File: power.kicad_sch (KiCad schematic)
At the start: 58 parts, among them U3 AP2112K-3.3, U4 LM317_TO-252, U5 LMR36520FADDA, U6 CJ431, U8 CJ431, U9 LMR36520FADDA

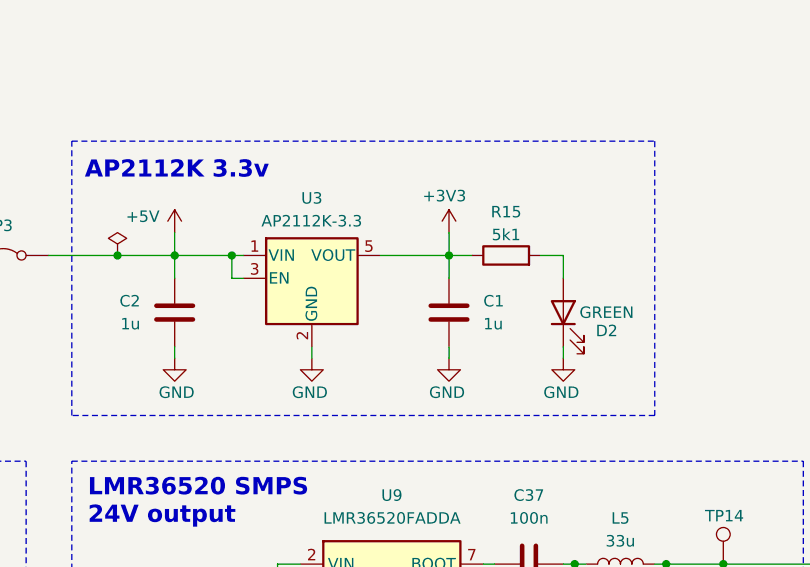
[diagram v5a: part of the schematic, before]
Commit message: schem: add +3V3 test point
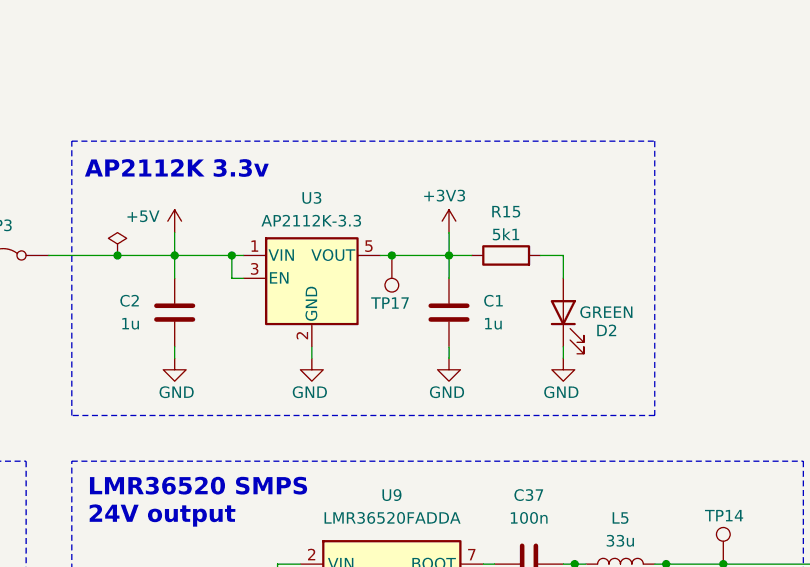
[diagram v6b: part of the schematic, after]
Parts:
- added TP17: TestPoint, symbol Connector:TestPoint
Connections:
- net +3V3: now also TP17.1
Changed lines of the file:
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@@
 	)
 	(junction
+		(at 213.36 91.44)
+		(diameter 0)
+		(color 0 0 0 0)
+	)
+	(junction
 		(at 100.33 128.27)
 		(diameter 0)
@@
 	(wire
 		(pts
+			(xy 213.36 91.44) (xy 219.71 91.44)
+		)
+		(stroke
+			(width 0)
+			(type default)
+		)
+	)
+	(wire
+		(pts
 			(xy 109.22 49.53) (xy 109.22 57.15)
 		)
@@
 	(wire
 		(pts
-			(xy 212.09 91.44) (xy 219.71 91.44)
+			(xy 212.09 91.44) (xy 213.36 91.44)
 		)
 		(stroke
@@
 					(unit 1)
 				)
+			)
+		)
+	)
+	(symbol
+		(lib_id "Connector:TestPoint")
+		(at 213.36 91.44 180)
+		(unit 1)
+		(exclude_from_sim no)
+		(in_bom yes)
+		(on_board yes)
+		(dnp no)
+		(property "Reference" "TP17"
+			(at 215.392 96.774 0)
+			(effects
+				(font
+					(size 1.27 1.27)
+				)
+				(justify left)
+			)
+		)
+		(property "Value" "TestPoint"
+			(at 210.82 93.4721 0)
+			(effects
+				(font
+					(size 1.27 1.27)
+				)
+				(justify left)
+				(hide yes)
+			)
+		)
+		(property "Footprint" ""
+			(at 208.28 91.44 0)
+			(effects
+				(font
+					(size 1.27 1.27)
+				)
+				(hide yes)
+			)
+		)
+		(property "Datasheet" "~"
+			(at 208.28 91.44 0)
+			(effects
+				(font
+					(size 1.27 1.27)
+				)
+				(hide yes)
+			)
+		)
+		(property "Description" "test point"
+			(at 213.36 91.44 0)
+			(effects
+				(font
+					(size 1.27 1.27)
+				)
+				(hide yes)
+			)
+		)
+		(pin "1"
+		)
+		(instances
+			(project "esp32c6-sensor-devboard"
+				(path "/f6edeef8-7fa0-4f55-9ad8-145372f41e3e/4befa429-10a8-402a-b91d-1560a39651d5"
+					(reference "TP17")
+					(unit 1)
+				)

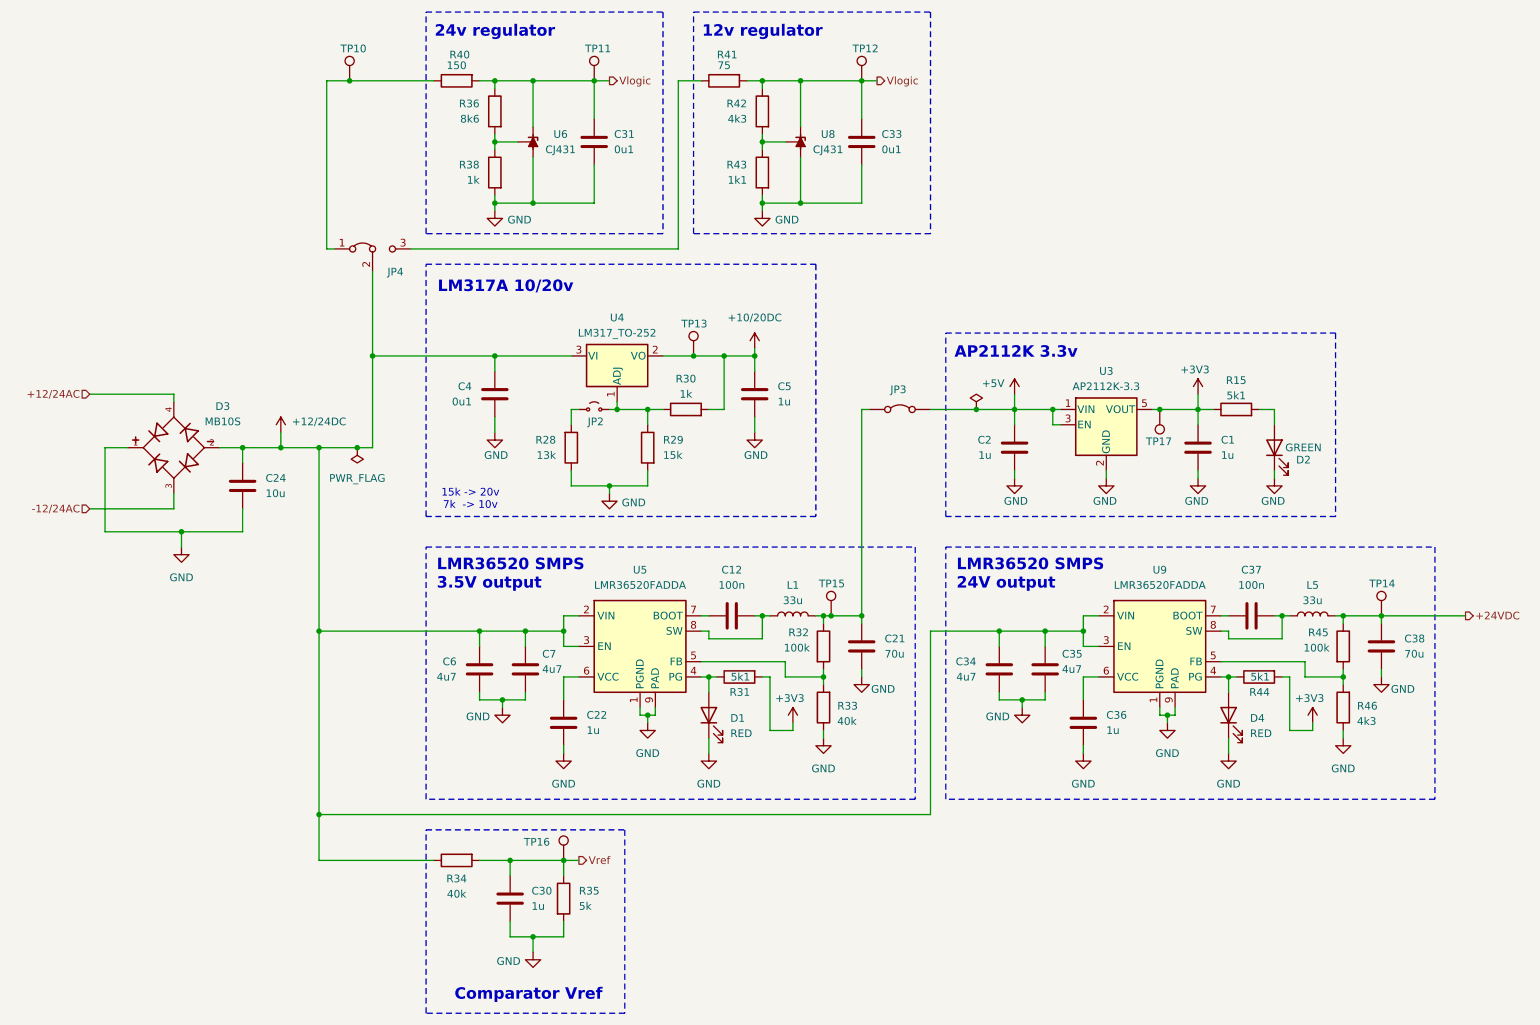
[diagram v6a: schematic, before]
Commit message: schem: assign footprints
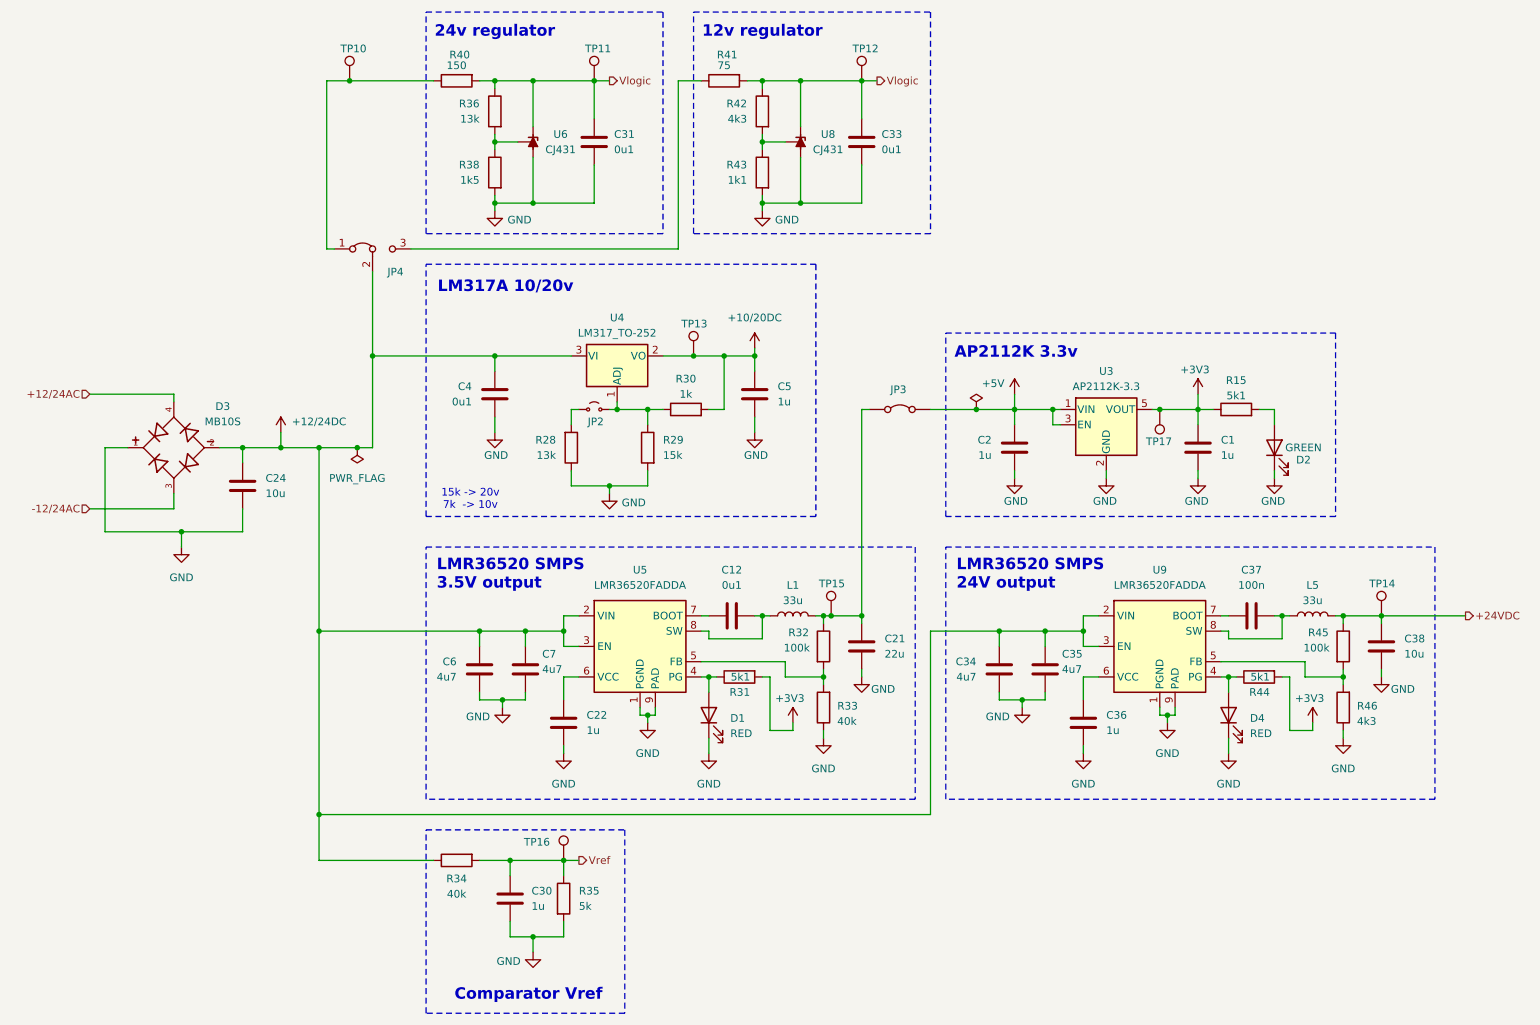
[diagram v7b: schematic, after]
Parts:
- C1, C2, C24, C4, C5: footprint (none) -> Capacitor_SMD:C_0603_1608Metric
- C12: value 100n -> 0u1; footprint (none) -> Capacitor_SMD:C_0402_1005Metric
- C21: value 70u -> 22u; footprint (none) -> Capacitor_SMD:C_0603_1608Metric
- C22, C30, C31, C33, C36, C37: footprint (none) -> Capacitor_SMD:C_0402_1005Metric
- C34, C35, C6, C7: footprint (none) -> Capacitor_SMD:C_1206_3216Metric
- C38: value 70u -> 10u; footprint (none) -> Capacitor_SMD:C_0603_1608Metric
- D1, D4: footprint (none) -> LED_SMD:LED_0603_1608Metric
- JP2, JP3: footprint (none) -> Connector_PinHeader_2.54mm:PinHeader_1x02_P2.54mm_Vertical
- JP4: footprint (none) -> Connector_PinHeader_2.54mm:PinHeader_1x03_P2.54mm_Vertical
- L1, L5: footprint (none) -> Inductor_SMD:L_Chilisin_BMRx00060630
- R15, R28, R29, R30, R31, R32, R33, R34, R35, R42, R43, R44, R45, R46: footprint (none) -> Resistor_SMD:R_0603_1608Metric
- R36: value 8k6 -> 13k; footprint (none) -> Resistor_SMD:R_0603_1608Metric
- R38: value 1k -> 1k5; footprint (none) -> Resistor_SMD:R_0603_1608Metric
- R40, R41: footprint (none) -> Resistor_SMD:R_0805_2012Metric
- TP10, TP11, TP12, TP13, TP14, TP15, TP16, TP17: footprint (none) -> TestPoint:TestPoint_Pad_D2.0mm
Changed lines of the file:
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@@
 			)
 		)
-		(property "Footprint" ""
+		(property "Footprint" "TestPoint:TestPoint_Pad_D2.0mm"
 			(at 255.27 125.73 0)
 			(effects
@@
 			)
 		)
-		(property "Footprint" ""
+		(property "Footprint" "Resistor_SMD:R_0805_2012Metric"
 			(at 140.97 35.052 90)
 			(effects
@@
 			)
 		)
-		(property "Footprint" ""
+		(property "Footprint" "Resistor_SMD:R_0603_1608Metric"
 			(at 113.792 97.79 90)
 			(effects
@@
 			)
 		)
-		(property "Footprint" ""
+		(property "Footprint" "Connector_PinHeader_2.54mm:PinHeader_1x02_P2.54mm_Vertical"
 			(at 119.38 91.44 0)
 			(effects
@@
 			)
 		)
-		(property "Value" "8k6"
+		(property "Value" "13k"
 			(at 100.33 43.1799 0)
 			(effects
@@
 			)
 		)
-		(property "Footprint" ""
+		(property "Footprint" "Resistor_SMD:R_0603_1608Metric"
 			(at 104.648 41.91 90)
 			(effects
@@
 			)
 		)
-		(property "Footprint" ""
+		(property "Footprint" "Resistor_SMD:R_0603_1608Metric"
 			(at 96.52 164.592 90)
 			(effects
@@
 			)
 		)
-		(property "Footprint" ""
+		(property "Footprint" "TestPoint:TestPoint_Pad_D2.0mm"
 			(at 140.97 82.55 0)
 			(effects
@@
 			)
 		)
-		(property "Footprint" ""
+		(property "Footprint" "Capacitor_SMD:C_0402_1005Metric"
 			(at 106.3752 176.53 0)
 			(effects
@@
 			)
 		)
-		(property "Footprint" ""
+		(property "Footprint" "Capacitor_SMD:C_1206_3216Metric"
 			(at 108.9152 138.43 0)
 			(effects
@@
 			)
 		)
-		(property "Footprint" ""
+		(property "Footprint" "Resistor_SMD:R_0603_1608Metric"
 			(at 226.06 93.218 90)
 			(effects
@@
 			)
 		)
-		(property "Footprint" ""
+		(property "Footprint" "Capacitor_SMD:C_0603_1608Metric"
 			(at 220.6752 101.6 0)
 			(effects
@@
 			)
 		)
-		(property "Footprint" ""
+		(property "Footprint" "Resistor_SMD:R_0603_1608Metric"
 			(at 245.618 140.97 90)
 			(effects
@@
 			)
 		)
-		(property "Footprint" ""
+		(property "Footprint" "TestPoint:TestPoint_Pad_D2.0mm"
 			(at 119.38 166.37 0)
 			(effects
@@
 			)
 		)
-		(property "Footprint" ""
+		(property "Footprint" "LED_SMD:LED_0603_1608Metric"
 			(at 224.79 142.24 0)
 			(effects
@@
 			)
 		)
-		(property "Footprint" ""
+		(property "Footprint" "TestPoint:TestPoint_Pad_D2.0mm"
 			(at 163.83 125.73 0)
 			(effects
@@
 			)
 		)
-		(property "Value" "1k"
+		(property "Value" "1k5"
 			(at 100.33 53.3399 0)
 			(effects
@@
 			)
 		)
-		(property "Footprint" ""
+		(property "Footprint" "Resistor_SMD:R_0603_1608Metric"
 			(at 104.648 52.07 90)
 			(effects
@@
 			)
 		)
-		(property "Footprint" ""
+		(property "Footprint" "Capacitor_SMD:C_0402_1005Metric"
 			(at 224.79 124.7648 0)
 			(effects
@@
 			)
 		)
-		(property "Footprint" ""
+		(property "Footprint" "Capacitor_SMD:C_0402_1005Metric"
 			(at 199.6948 147.32 0)
 			(effects
@@
 			)
 		)
-		(property "Footprint" ""
+		(property "Footprint" "Connector_PinHeader_2.54mm:PinHeader_1x02_P2.54mm_Vertical"
 			(at 170.18 91.44 0)
 			(effects
@@
 			)
 		)
-		(property "Footprint" ""
+		(property "Footprint" "Resistor_SMD:R_0603_1608Metric"
 			(at 149.098 41.91 90)
 			(effects
@@
 			)
 		)
-		(property "Footprint" ""
+		(property "Footprint" "Resistor_SMD:R_0603_1608Metric"
 			(at 112.522 172.72 90)
 			(effects
@@
 			)
 		)
-		(property "Footprint" ""
+		(property "Footprint" "Capacitor_SMD:C_1206_3216Metric"
 			(at 195.2752 138.43 0)
 			(effects
@@
 			)
 		)
-		(property "Footprint" ""
+		(property "Footprint" "Capacitor_SMD:C_1206_3216Metric"
 			(at 99.3648 138.43 0)
 			(effects
@@
 			)
 		)
-		(property "Footprint" ""
+		(property "Footprint" "TestPoint:TestPoint_Pad_D2.0mm"
 			(at 83.82 36.83 0)
 			(effects
@@
 			)
 		)
-		(property "Footprint" ""
+		(property "Footprint" "Capacitor_SMD:C_0402_1005Metric"
 			(at 120.3452 50.8 0)
 			(effects
@@
 			)
 		)
-		(property "Value" "70u"
+		(property "Value" "22u"
 			(at 167.64 132.0799 0)
 			(effects
@@
 			)
 		)
-		(property "Footprint" ""
+		(property "Footprint" "Capacitor_SMD:C_0603_1608Metric"
 			(at 162.8648 127 0)
 			(effects
@@
 			)
 		)
-		(property "Footprint" ""
+		(property "Footprint" "Capacitor_SMD:C_0402_1005Metric"
 			(at 164.7952 50.8 0)
 			(effects
@@
 			)
 		)
-		(property "Footprint" ""
+		(property "Footprint" "Resistor_SMD:R_0603_1608Metric"
 			(at 130.048 97.79 90)
 			(effects
@@
 			)
 		)
-		(property "Value" "100n"
+		(property "Value" "0u1"
 			(at 142.24 120.65 90)
 			(effects
@@
 			)
 		)
-		(property "Footprint" ""
+		(property "Footprint" "Capacitor_SMD:C_0402_1005Metric"
 			(at 138.43 124.7648 0)
 			(effects
@@
 			)
 		)
-		(property "Footprint" ""
+		(property "Footprint" "Capacitor_SMD:C_0603_1608Metric"
 			(at 61.9252 107.95 0)
 			(effects
@@
 			)
 		)
-		(property "Value" "70u"
+		(property "Value" "10u"
 			(at 254 132.0799 0)
 			(effects
@@
 			)
 		)
-		(property "Footprint" ""
+		(property "Footprint" "Capacitor_SMD:C_0603_1608Metric"
 			(at 249.2248 127 0)
 			(effects
@@
 			)
 		)
-		(property "Footprint" ""
+		(property "Footprint" "TestPoint:TestPoint_Pad_D2.0mm"
 			(at 124.46 36.83 0)
 			(effects
@@
 			)
 		)
-		(property "Footprint" ""
+		(property "Footprint" "Capacitor_SMD:C_0603_1608Metric"
 			(at 101.9048 92.71 0)
 			(effects
@@
 			)
 		)
-		(property "Footprint" ""
+		(property "Footprint" "Resistor_SMD:R_0603_1608Metric"
 			(at 149.098 52.07 90)
 			(effects
@@
 			)
 		)
-		(property "Footprint" ""
+		(property "Footprint" "Inductor_SMD:L_Chilisin_BMRx00060630"
 			(at 152.4 125.73 0)
 			(effects
@@
 			)
 		)
-		(property "Footprint" ""
+		(property "Footprint" "Capacitor_SMD:C_0402_1005Metric"
 			(at 113.3348 147.32 0)
 			(effects
@@
 			)
 		)
-		(property "Footprint" ""
+		(property "Footprint" "TestPoint:TestPoint_Pad_D2.0mm"
 			(at 168.91 36.83 0)
 			(effects
@@
 			)
 		)
-		(property "Footprint" ""
+		(property "Footprint" "Resistor_SMD:R_0603_1608Metric"
 			(at 229.87 134.112 90)
 			(effects
@@
 			)
 		)
-		(property "Footprint" ""
+		(property "Footprint" "Connector_PinHeader_2.54mm:PinHeader_1x03_P2.54mm_Vertical"
 			(at 82.55 64.77 0)
 			(effects
@@
 			)
 		)
-		(property "Footprint" ""
+		(property "Footprint" "Resistor_SMD:R_0805_2012Metric"
 			(at 96.52 35.052 90)
 			(effects
@@
 			)
 		)
-		(property "Footprint" ""
+		(property "Footprint" "Inductor_SMD:L_Chilisin_BMRx00060630"
 			(at 238.76 125.73 0)
 			(effects
@@
 			)
 		)
-		(property "Footprint" ""
+		(property "Footprint" "TestPoint:TestPoint_Pad_D2.0mm"
 			(at 208.28 91.44 0)
 			(effects
@@
 			)
 		)
-		(property "Footprint" ""
+		(property "Footprint" "Capacitor_SMD:C_0603_1608Metric"
 			(at 188.2648 101.6 0)
 			(effects
@@
 			)
 		)
-		(property "Footprint" ""
+		(property "Footprint" "Resistor_SMD:R_0603_1608Metric"
 			(at 143.51 134.112 90)
 			(effects
@@
 			)
 		)
-		(property "Footprint" ""
+		(property "Footprint" "LED_SMD:LED_0603_1608Metric"
 			(at 138.43 142.24 0)
 			(effects
@@
 			)
 		)
-		(property "Footprint" ""
+		(property "Footprint" "Resistor_SMD:R_0603_1608Metric"
 			(at 159.258 140.97 90)
 			(effects
@@
 			)
 		)
-		(property "Footprint" ""
+		(property "Footprint" "Capacitor_SMD:C_0603_1608Metric"
 			(at 147.0152 92.71 0)
 			(effects
@@
 			)
 		)
-		(property "Footprint" ""
+		(property "Footprint" "Resistor_SMD:R_0603_1608Metric"
 			(at 155.702 130.81 90)
 			(effects
@@
 			)
 		)
-		(property "Footprint" ""
+		(property "Footprint" "Resistor_SMD:R_0603_1608Metric"
 			(at 242.062 130.81 90)
 			(effects
@@
 			)
 		)
-		(property "Footprint" ""
+		(property "Footprint" "Resistor_SMD:R_0603_1608Metric"
 			(at 134.62 93.218 90)
 			(effects
@@
 			)
 		)
-		(property "Footprint" ""
+		(property "Footprint" "Capacitor_SMD:C_1206_3216Metric"
 			(at 185.7248 138.43 0)
 			(effects

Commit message: schem: add part numbers to BOM
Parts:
- C1, C2, C5: Basic (none) -> Y; JLCPCB Part # (none) -> C15849; Manufacturer (none) -> Samsung Electro-Mechanics; Manufacturer Part Number (none) -> CL10A105KB8NNNC
- C12, C31, C33, C37: Basic (none) -> Y; JLCPCB Part # (none) -> C307331; Manufacturer (none) -> Samsung Electro-Mechanics; Manufacturer Part Number (none) -> CL05B104KB54PNC
- C21: Basic (none) -> Y; JLCPCB Part # (none) -> C59461; Manufacturer (none) -> Samsung Electro-Mechanics; Manufacturer Part Number (none) -> CL10A226MQ8NRNC
- C22, C30, C36: Basic (none) -> Y; JLCPCB Part # (none) -> C52923; Manufacturer (none) -> Samsung Electro-Mechanics; Manufacturer Part Number (none) -> CL05A105KA5NQNC
- C24: footprint Capacitor_SMD:C_0603_1608Metric -> Capacitor_SMD:C_0805_2012Metric; Basic (none) -> Y; JLCPCB Part # (none) -> C440198; Manufacturer (none) -> Murata; Manufacturer Part Number (none) -> GRM21BR61H106KE43L
- C34, C35, C6, C7: Basic (none) -> Y; JLCPCB Part # (none) -> C29823; Manufacturer (none) -> Guangdong Fenghua Advanced Tech (FH); Manufacturer Part Number (none) -> 1206B475K500NT
- C38: Basic (none) -> Y; JLCPCB Part # (none) -> C96446; Manufacturer (none) -> Samsung Electro-Mechanics; Manufacturer Part Number (none) -> CL10A106MA8NRNC
- C4: Basic (none) -> Y; JLCPCB Part # (none) -> C14663; Manufacturer (none) -> YAGEO; Manufacturer Part Number (none) -> CC0603KRX7R9BB104
- D1, D4: Basic (none) -> Y; JLCPCB Part # (none) -> C2286; Manufacturer (none) -> Hubei KENTO Elec; Manufacturer Part Number (none) -> KT-0603R
- D3: Basic (none) -> Y; JLCPCB Part # (none) -> C2488; Manufacturer (none) -> Microdiode Semiconductor (MDD); Manufacturer Part Number (none) -> C2488
- JP2, JP3, TP10, TP11, TP12, TP13, TP14, TP15, TP16, TP17: now left out of the parts list
